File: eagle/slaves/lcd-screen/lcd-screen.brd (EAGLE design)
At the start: 99.1 x 73.7 mm, 23 parts, among them CON1 SPI, IC1 MCP1703CB, J1 RJ12RIGHTANGLE-I2C, J2 RJ12RIGHTANGLE-I2C, J3 RJ12RIGHTANGLE-I2C, U1 ATMEGA328P_TQFP

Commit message: rename lcd-slave and add address selector
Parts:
- added SJ1, SJ2: (no value), jumper:SJ
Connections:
- net A6: now also SJ1.1
- net A7: now also SJ2.1
- net GND: now also SJ1.2, SJ2.2
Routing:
- net A7: track 0.00 -> 5.04 mm, vias 0 -> 1
- net A6: track 0.00 -> 5.03 mm, vias 0 -> 1
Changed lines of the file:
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@@
 <attribute name="MPN" value="621-1N5819HW-F" x="15.875" y="12.7" size="1.778" layer="27" rot="R270" display="off"/>
 </element>
+<element name="SJ1" library="jumper" library_urn="urn:adsk.eagle:library:252" package="SJ" package3d_urn="urn:adsk.eagle:package:15471/1" value="" x="31.75" y="29.21" rot="MR90"/>
+<element name="SJ2" library="jumper" library_urn="urn:adsk.eagle:library:252" package="SJ" package3d_urn="urn:adsk.eagle:package:15471/1" value="" x="29.21" y="29.21" rot="MR90"/>
 </elements>
 <signals>
@@
 <wire x1="20.955" y1="27.035" x2="20.955" y2="26.67" width="0.635" layer="1"/>
 <via x="20.955" y="26.67" extent="1-16" drill="0.5"/>
+<contactref element="SJ1" pad="2"/>
+<contactref element="SJ2" pad="2"/>
 </signal>
 <signal name="SCK">
@@
 <wire x1="22.225" y1="23.495" x2="21.423" y2="22.693" width="0.4064" layer="1"/>
 <wire x1="21.423" y1="22.693" x2="21.423" y2="16.677" width="0.4064" layer="1"/>
+<wire x1="21.423" y1="17.54996875" x2="22.5366625" y2="19.9046" width="0" layer="19" extent="1-1"/>
+<wire x1="21.423" y1="16.677" x2="21.43125" y2="17.54171875" width="0" layer="19" extent="1-1"/>
 </signal>
 <signal name="VCC">
@@
 <signal name="A6">
 <contactref element="U1" pad="19"/>
+<contactref element="SJ1" pad="1"/>
+<wire x1="29.775" y1="24.6126" x2="29.775" y2="26.6" width="0.4064" layer="1"/>
+<wire x1="29.775" y1="26.6" x2="29.845" y2="26.67" width="0.4064" layer="1"/>
+<via x="29.845" y="26.67" extent="1-16" drill="0.35"/>
+<wire x1="29.845" y1="26.67" x2="30.48" y2="27.305" width="0.4064" layer="16"/>
+<wire x1="30.48" y1="27.305" x2="31.115" y2="27.305" width="0.4064" layer="16"/>
+<wire x1="31.115" y1="27.305" x2="31.75" y2="27.94" width="0.4064" layer="16"/>
+<wire x1="31.75" y1="27.94" x2="31.75" y2="28.448" width="0.4064" layer="16"/>
 </signal>
 <signal name="A7">
 <contactref element="U1" pad="22"/>
+<contactref element="SJ2" pad="1"/>
+<wire x1="27.375" y1="24.6126" x2="27.375" y2="25.48916875" width="0.4064" layer="1"/>
+<via x="27.375" y="25.48916875" extent="1-16" drill="0.35"/>
+<wire x1="27.375" y1="25.48916875" x2="27.67998125" y2="25.79415" width="0.4064" layer="16"/>
+<wire x1="27.67998125" y1="25.79415" x2="28.4411375" y2="25.79415" width="0.4064" layer="16"/>
+<wire x1="28.4411375" y1="25.79415" x2="29.0644" y2="26.4174125" width="0.4064" layer="16"/>
+<wire x1="29.0644" y1="26.9933375" x2="29.21" y2="27.1389375" width="0.4064" layer="16"/>
+<wire x1="29.21" y1="27.1389375" x2="29.21" y2="28.448" width="0.4064" layer="16"/>
+<wire x1="29.0644" y1="26.4174125" x2="29.0644" y2="26.9933375" width="0.4064" layer="16"/>
 </signal>
 <signal name="EXT-FTDI">

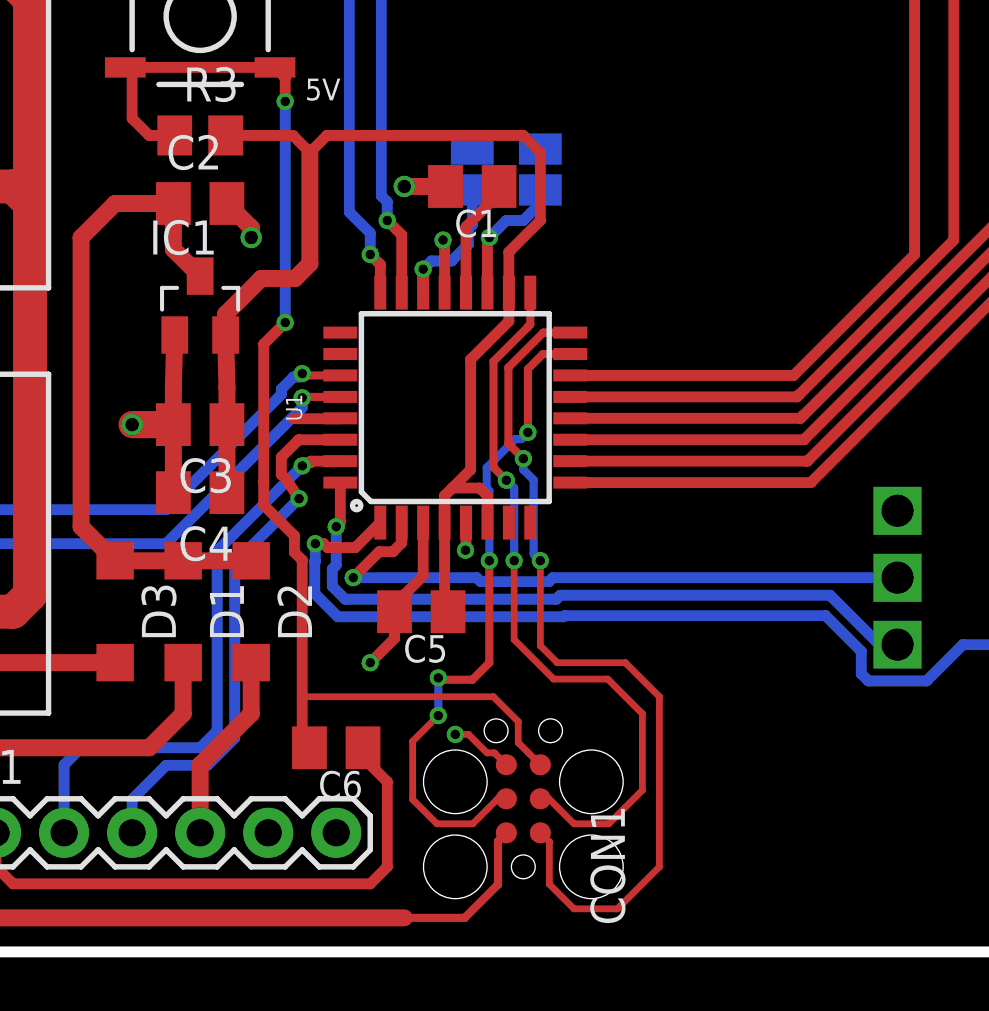
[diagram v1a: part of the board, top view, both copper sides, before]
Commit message: add crystal to bard
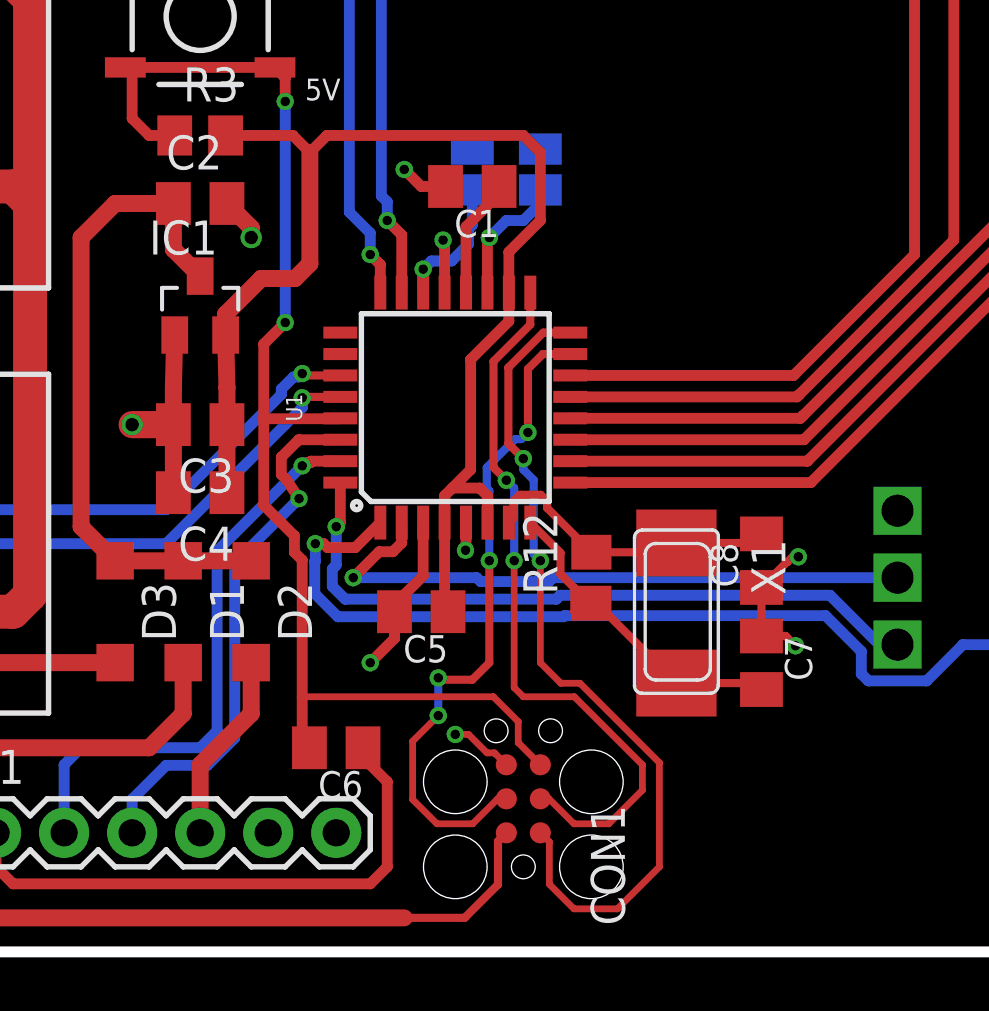
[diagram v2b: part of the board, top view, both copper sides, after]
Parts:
- added C7, C8: 18pF, rcl:C0805K
- added R12: 1M, rcl:R0805
- added X1: 8MHz, lpatiny:NX6035
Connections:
- net EXT-FTDI renamed VCC-FTDI
- net EXT-VCC renamed VCC-ICSP
- new net N$42: C8.2, R12.2, U1.7, X1.P$2
- new net XTAL1: C7.2, R12.1, U1.8, X1.P$1
- net GND: now also C7.1, C8.1
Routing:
- net XTAL1: track 0.00 -> 12.5 mm
- net N$42: track 0.00 -> 11.6 mm
- net GND: track 29.7 -> 35.0 mm, vias 9 -> 11
- net RESET: track 48.2 -> 49.3 mm
- net MISO: track 32.5 -> 31.4 mm

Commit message: submitted lcd-screen design
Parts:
- SJ1: value (none) -> A0
- SJ2: value (none) -> A1
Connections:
- removed net N$42: C8.2, R12.2, U1.7, X1.P$2
- new net XTAL2: C7.2, R12.1, U1.8, X1.P$1
- net XTAL1: now also C8.2, R12.2, U1.7, X1.P$2; no longer C7.2, R12.1, U1.8, X1.P$1
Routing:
- net XTAL2: track 0.00 -> 12.5 mm
- net N$42: track 11.6 -> 0.00 mm
- net XTAL1: track 12.5 -> 11.6 mm
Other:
- board text added: "A0"
- board text added: "A1"
